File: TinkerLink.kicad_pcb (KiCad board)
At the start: 2 copper layers, 40 x 20 mm, 19 parts, among them J1 Conn_01x06_Pin, Q1 IRF4905S, Q2 MMBT2222A, SW1 TS-061D-250D4-P, U1 ESP-01F-2M, U2 ME6211C33M5

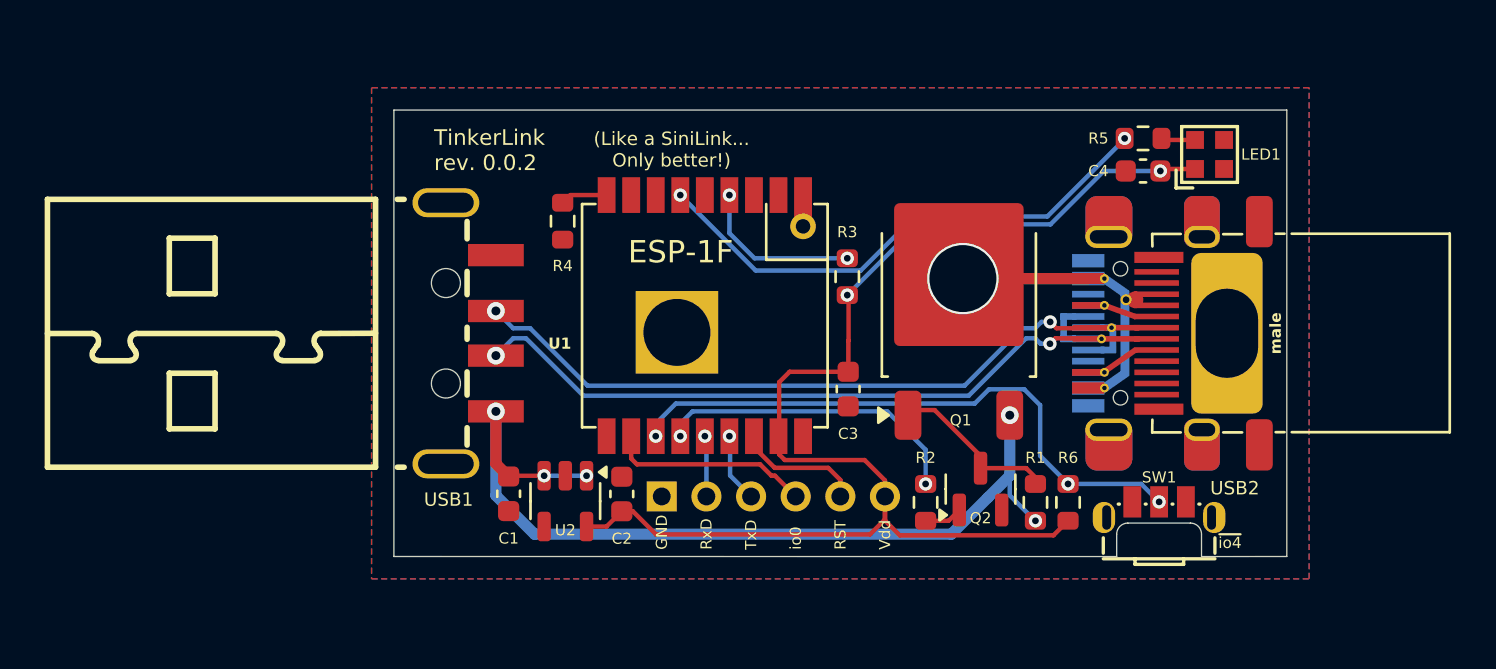
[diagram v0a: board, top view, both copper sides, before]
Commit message: Layout squeezed to the right
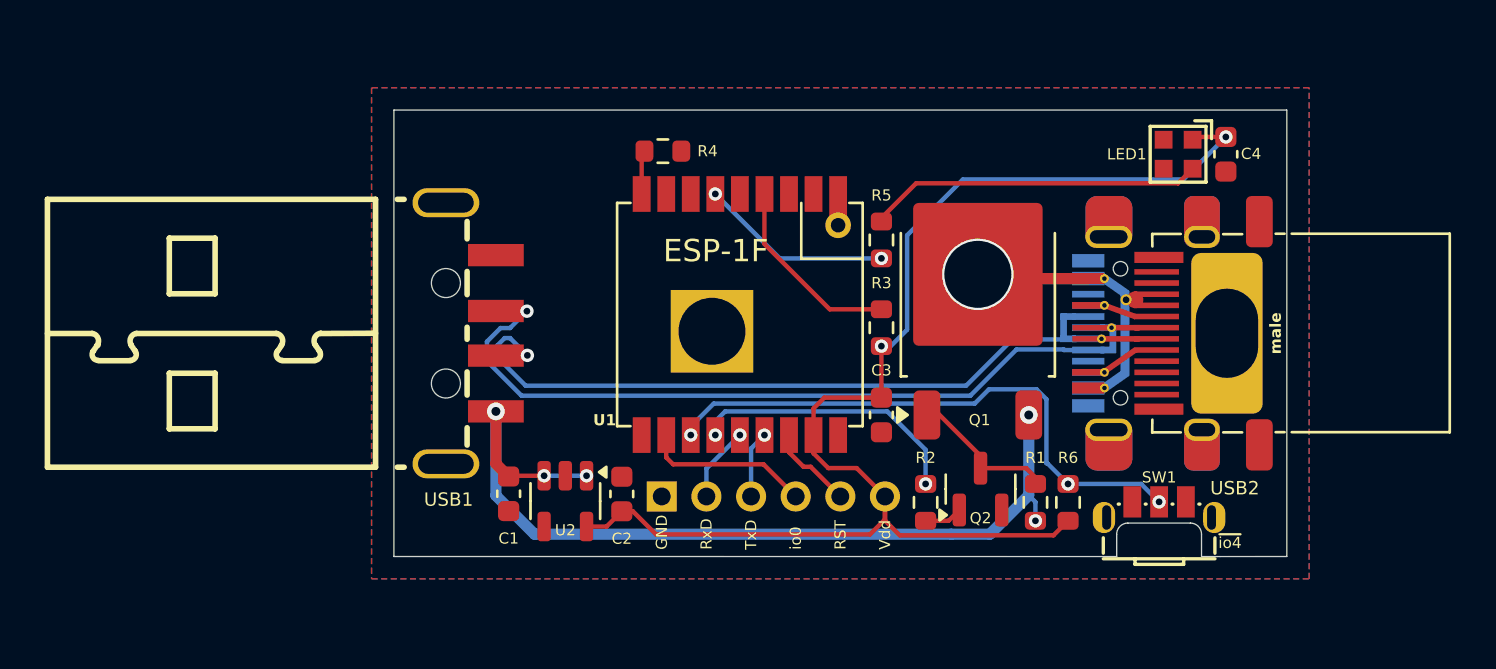
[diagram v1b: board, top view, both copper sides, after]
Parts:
- moved R5 12.6 mm to (101.8, 95.8), turned to -90 degrees
- moved R4 5.48 mm to (92.0, 91.8), turned to 0 degrees
- moved C4 3.79 mm to (117.3, 92.0), turned to -90 degrees
- moved R3 2.75 mm to (101.8, 99.8)
- moved C3 1.89 mm to (101.8, 103.7)
- moved U1 1.57 mm to (95.5, 99.2)
- moved LED1 1.41 mm to (115.1, 92.0), turned to 90 degrees
- moved Q1 0.85 mm to (106.2, 98.6)
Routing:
- net io14: track 23.8 -> 8.68 mm
- net Net-(LED1-DIN): track 1.53 -> 15.0 mm
- net /RST: track 5.71 -> 3.89 mm
- net /D+: track 30.0 -> 31.7 mm, vias 2 -> 1
- net i05: track 14.0 -> 12.5 mm
- net /io0: track 9.07 -> 7.52 mm
- net /VbusS: track 11.5 -> 10.0 mm
- net io4: track 27.2 -> 25.8 mm
- net /EN: track 7.45 -> 8.69 mm, vias 2 -> 0
- net Vdd: track 59.1 -> 60.1 mm
- net Net-(Q1-G): track 7.67 -> 6.81 mm
- net /Rx: track 2.73 -> 3.37 mm
- net /D-: track 30.0 -> 30.2 mm, vias 2 -> 1

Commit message: fiddlin' with silscreen
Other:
- board text added: "${TITLE} rev. ${REVISION}"
- board text removed: "TinkerLink rev. 0.0.2"
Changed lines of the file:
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@@
 	)
 	(paper "A4")
+	(title_block
+		(title "TinkerLink")
+		(rev "0.0.2")
+	)
 	(layers
 		(0 "F.Cu" signal)
@@
 		)
 	)
-	(gr_text "TinkerLink\nrev. 0.0.2"
+	(gr_text "${TITLE}\nrev. ${REVISION}"
 		(at 108.62 91.5 0)
 		(layer "B.SilkS")

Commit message: Bloody Rabbit Hole Sub-Basement!
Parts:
- added Rshunt: 0R1 1%, Resistor_SMD:R_2512_6332Metric, F.Cu at (86.5, 109.7)
- USB1: value USB-212-BCW -> USB-A-USB-C; footprint LCSCfootprints:USB-A-SMD_USB-212-BCW -> tinker:USB-A-USB-C
- moved C1 23.4 mm to (108.4, 109.9)
- moved U2 18.4 mm to (105.9, 109.9), turned to 90 degrees
- moved C2 13.6 mm to (103.5, 109.9), turned to -90 degrees
- moved C4 2.26 mm to (115.2, 92.8), turned to 180 degrees
- moved SW1 2.00 mm to (114.3, 110.0)
- moved LED1 1.62 mm to (115.2, 90.4), turned to 0 degrees
- moved R1 1.53 mm to (108.4, 106.1)
- moved R2 1.52 mm to (103.5, 106.1)
- moved Q2 1.52 mm to (106.0, 105.5)
- moved Q1 1.45 mm to (106.1, 97.2)
- moved R5 1.22 mm to (101.8, 94.6)
- moved R3 1.04 mm to (101.8, 98.7)
- moved R4 1.00 mm to (92.0, 90.8)
- moved U1 1.00 mm to (95.5, 98.2)
- moved C3 0.90 mm to (101.9, 102.8)
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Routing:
- net Vdd: track 60.1 -> 45.2 mm
- net /D+: track 31.7 -> 25.2 mm, vias 1 -> 0
- net /D-: track 30.2 -> 25.3 mm, vias 1 -> 0
- net io4: track 25.8 -> 29.3 mm
- net /Vbus: track 40.6 -> 38.3 mm
- net /VbusS: track 10.0 -> 12.2 mm
- net /Rx: track 3.37 -> 5.33 mm
- net /Tx: track 3.00 -> 4.90 mm
- net /RST: track 3.89 -> 5.19 mm
- net /io0: track 7.52 -> 8.49 mm
- net Net-(Q1-G): track 6.81 -> 5.96 mm
- net /EN: track 8.69 -> 9.26 mm
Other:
- board size 40 x 20 mm -> 40 x 24 mm

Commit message: Tweakin' (NOT twerkin') coz Austin hasn't admitted to doin' anything yet...
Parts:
- moved Rshunt 0.15 mm to (86.4, 109.7)
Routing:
- net /Vbus: track 38.3 -> 39.4 mm, vias 5 -> 7
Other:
- board text added: "~{RST}"
- board text added: "~{io0}"
- board text removed: "RST"
- board text removed: "io0"
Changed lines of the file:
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@@
 	(footprint "Resistor_SMD:R_2512_6332Metric"
 		(layer "F.Cu")
-		(at 86.55 109.66)
+		(at 86.4 109.66)
 		(descr "Resistor SMD 2512 (6332 Metric), square (rectangular) end terminal, IPC-7351 nominal, (Body size source: IPC-SM-782 page 72, https://www.pcb-3d.com/wordpress/wp-content/uploads/ipc-sm-782a_amendment_1_and_2.pdf), generated with kicad-footprint-generator")
 		(tags "resistor")
@@
 		)
 	)
-	(gr_text "RST"
+	(gr_text "~{RST}"
 		(at 99.5 109 90)
 		(layer "F.SilkS")
@@
 		)
 	)
-	(gr_text "io0"
+	(gr_text "~{io0}"
 		(at 97.5 109 90)
 		(layer "F.SilkS")
@@
 		)
 	)
+	(segment
+		(start 84.51 109.66)
+		(end 88.29 109.66)
+		(width 0.5)
+		(layer "F.Cu")
+		(net 5)
+	)
+	(segment
+		(start 88.29 109.66)
+		(end 88.3 109.65)
+		(width 0.5)
+		(layer "F.Cu")
+		(net 5)
+	)
+	(via
+		(at 84.51 109.66)
+		(size 0.6)
+		(drill 0.3)
+		(layers "F.Cu" "B.Cu")
+		(net 5)
+	)
 	(via
 		(at 108.39 106.915)
@@
 		(net 5)
 	)
-	(segment
-		(start 84.51 103.14)
-		(end 84.51 107.8625)
-		(width 0.5)
-		(layer "B.Cu")
+	(via
+		(at 88.3 109.66)
+		(size 0.6)
+		(drill 0.3)
+		(layers "F.Cu" "B.Cu")
 		(net 5)
 	)
@@
 	)
 	(segment
-		(start 87.685 111.0375)
+		(start 89.6775 111.0375)
 		(end 104.9875 111.0375)
+		(width 0.5)
+		(layer "B.Cu")
+		(net 5)
+	)
+	(segment
+		(start 84.51 103.14)
+		(end 84.51 109.61)
 		(width 0.5)
 		(layer "B.Cu")
@@
 	)
 	(segment
+		(start 84.51 109.61)
+		(end 84.51 109.64)
+		(width 0.5)
+		(layer "B.Cu")
+		(net 5)
+	)
+	(segment
 		(start 104.9875 111.0375)
 		(end 106.8875 111.0375)
@@
 	)
 	(segment
-		(start 84.51 107.8625)
-		(end 87.685 111.0375)
-		(width 0.5)
-		(layer "B.Cu")
-		(net 5)
-	)
-	(segment
 		(start 108.39 109.12)
 		(end 108.39 109.535)
 		(width 0.5)
 		(layer "B.Cu")
+		(net 5)
+	)
+	(segment
+		(start 88.3 109.66)
+		(end 89.6775 111.0375)
+		(width 0.5)
+		(layer "B.Cu")
